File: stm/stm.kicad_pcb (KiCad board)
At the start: 2 copper layers, 28 parts, among them U2 STM32H730ZBTx, U3 LAN8742A, U4 LM1117MP-ADJ, U5 FT232RL

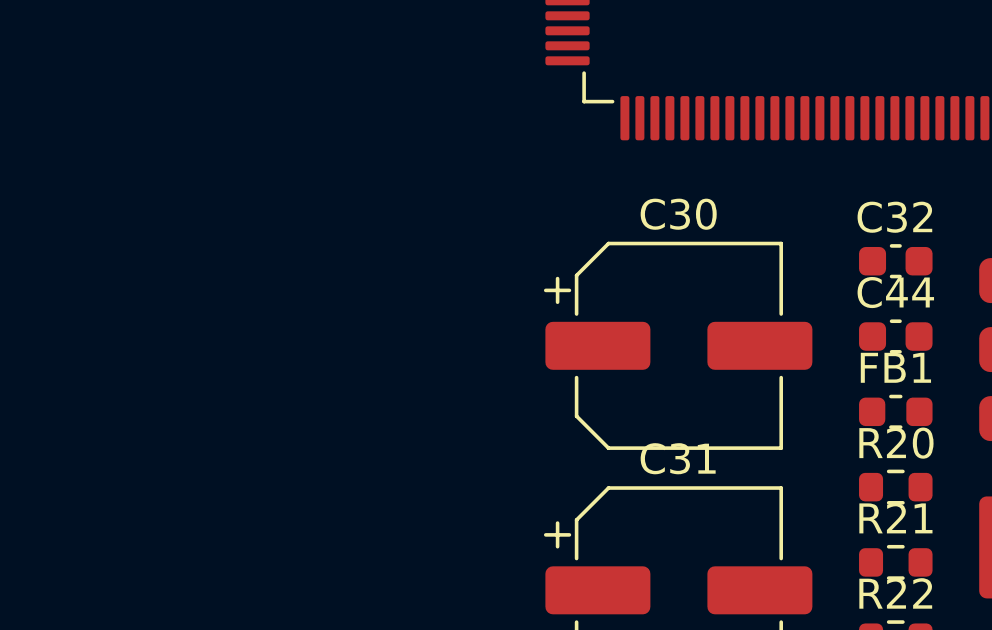
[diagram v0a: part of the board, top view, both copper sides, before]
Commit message: updated DAQ silkscreen to be less dumb
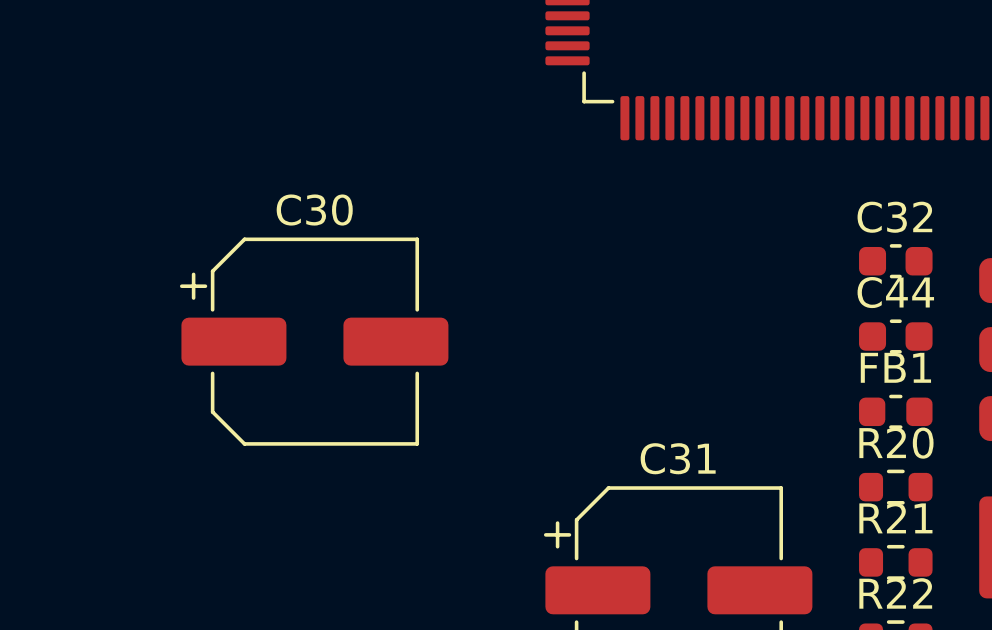
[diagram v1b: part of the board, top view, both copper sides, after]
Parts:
- moved C30 12.1 mm to (95.0, 104.0)
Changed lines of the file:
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@@
 	(footprint "Capacitor_SMD:CP_Elec_6.3x7.7"
 		(layer "F.Cu")
-		(at 107.1325 104.14)
+		(at 95 104)
 		(descr "SMD capacitor, aluminum electrolytic, Nichicon, 6.3x7.7mm")
 		(tags "capacitor electrolytic")

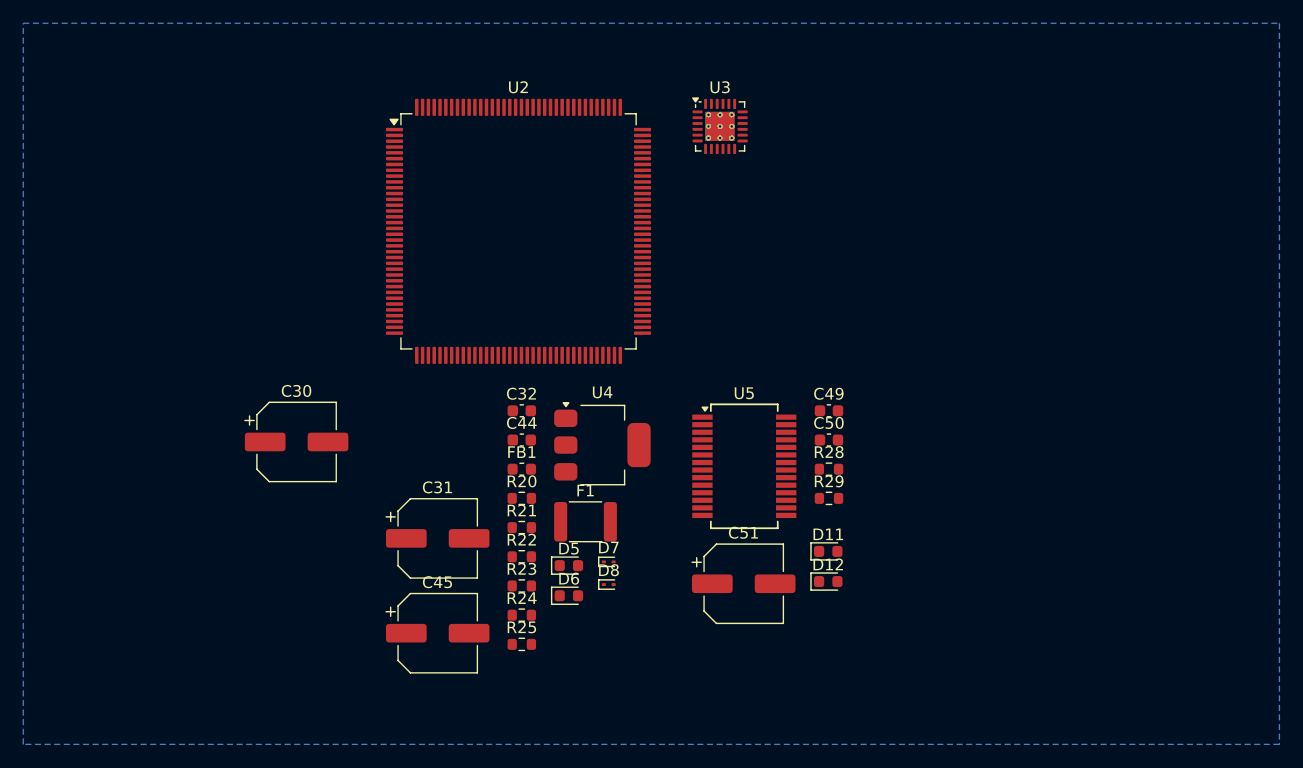
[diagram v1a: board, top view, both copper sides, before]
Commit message: Added components to main libs folder
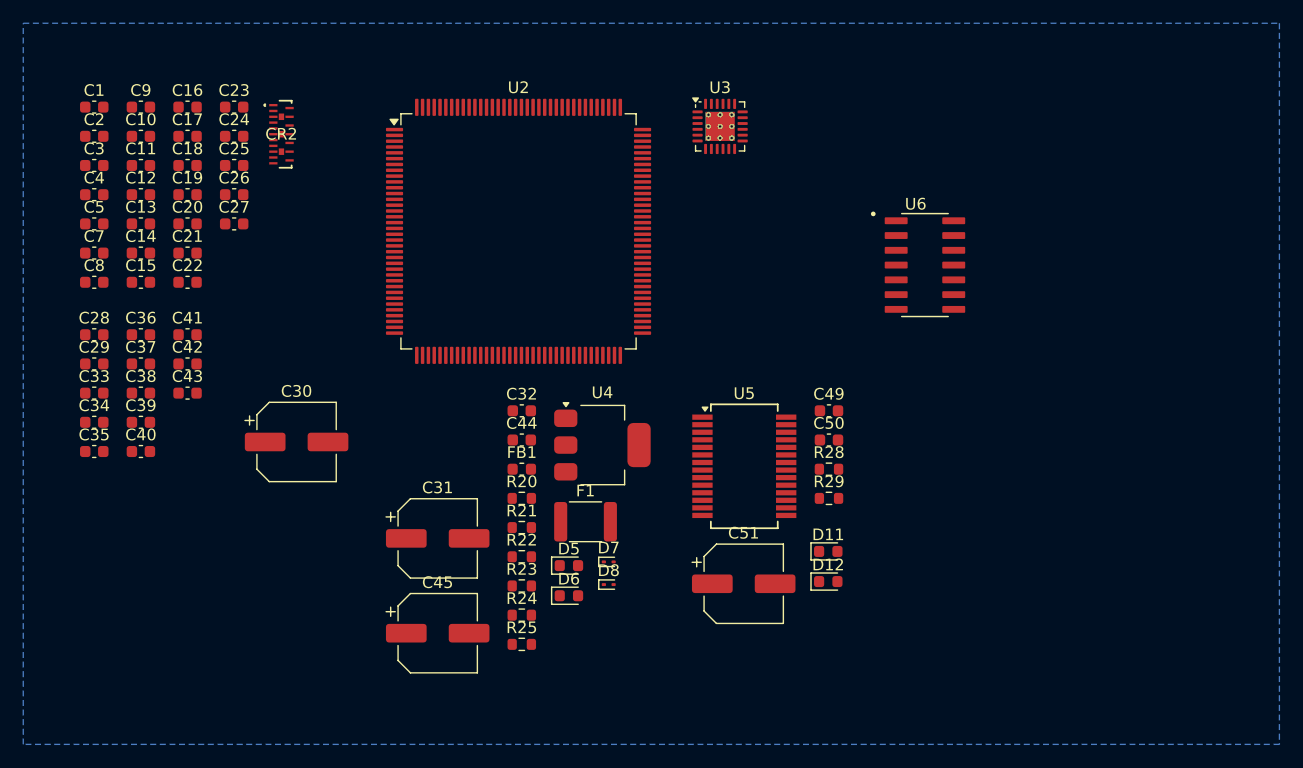
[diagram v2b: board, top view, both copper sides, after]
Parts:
- added C1: 100n, Capacitor_SMD:C_0603_1608Metric, F.Cu at (77.6, 75.2)
- added C10: 100n, Capacitor_SMD:C_0603_1608Metric, F.Cu at (81.6, 77.7)
- added C11: 2.2u, Capacitor_SMD:C_0603_1608Metric, F.Cu at (81.6, 80.2)
- added C12: 2.2u, Capacitor_SMD:C_0603_1608Metric, F.Cu at (81.6, 82.7)
- added C13: 15p, Capacitor_SMD:C_0603_1608Metric, F.Cu at (81.6, 85.2)
- added C14: 15p, Capacitor_SMD:C_0603_1608Metric, F.Cu at (81.6, 87.8)
- added C15: 100n, Capacitor_SMD:C_0603_1608Metric, F.Cu at (81.6, 90.3)
- added C16: 100n, Capacitor_SMD:C_0603_1608Metric, F.Cu at (85.6, 75.2)
- added C17: 100n, Capacitor_SMD:C_0603_1608Metric, F.Cu at (85.6, 77.7)
- added C18: 100n, Capacitor_SMD:C_0603_1608Metric, F.Cu at (85.6, 80.2)
- added C19: 100n, Capacitor_SMD:C_0603_1608Metric, F.Cu at (85.6, 82.7)
- added C2: 1u, Capacitor_SMD:C_0603_1608Metric, F.Cu at (77.6, 77.7)
- added C20: 1u, Capacitor_SMD:C_0603_1608Metric, F.Cu at (85.6, 85.2)
- added C21: 100n, Capacitor_SMD:C_0603_1608Metric, F.Cu at (85.6, 87.8)
- added C22: 100n, Capacitor_SMD:C_0603_1608Metric, F.Cu at (85.6, 90.3)
- added C23: 100n, Capacitor_SMD:C_0603_1608Metric, F.Cu at (89.6, 75.2)
- added C24: 100n, Capacitor_SMD:C_0603_1608Metric, F.Cu at (89.6, 77.7)
- added C25: 100n, Capacitor_SMD:C_0603_1608Metric, F.Cu at (89.6, 80.2)
- added C26: 100n, Capacitor_SMD:C_0603_1608Metric, F.Cu at (89.6, 82.7)
- added C27: 4u7, Capacitor_SMD:C_0603_1608Metric, F.Cu at (89.6, 85.2)
- added C28: C, Capacitor_SMD:C_0603_1608Metric, F.Cu at (77.6, 94.8)
- added C29: C, Capacitor_SMD:C_0603_1608Metric, F.Cu at (77.6, 97.3)
- added C3: 100n, Capacitor_SMD:C_0603_1608Metric, F.Cu at (77.6, 80.2)
- added C33: C, Capacitor_SMD:C_0603_1608Metric, F.Cu at (77.6, 99.8)
- added C34: C, Capacitor_SMD:C_0603_1608Metric, F.Cu at (77.6, 102.3)
- added C35: 470p, Capacitor_SMD:C_0603_1608Metric, F.Cu at (77.6, 104.8)
- added C36: 1u, Capacitor_SMD:C_0603_1608Metric, F.Cu at (81.6, 94.8)
- added C37: 1u, Capacitor_SMD:C_0603_1608Metric, F.Cu at (81.6, 97.3)
- added C38: 1u, Capacitor_SMD:C_0603_1608Metric, F.Cu at (81.6, 99.8)
- added C39: 10p, Capacitor_SMD:C_0603_1608Metric, F.Cu at (81.6, 102.3)
- added C4: 1u, Capacitor_SMD:C_0603_1608Metric, F.Cu at (77.6, 82.7)
- added C40: 10p, Capacitor_SMD:C_0603_1608Metric, F.Cu at (81.6, 104.8)
- added C41: 10p, Capacitor_SMD:C_0603_1608Metric, F.Cu at (85.6, 94.8)
- added C42: 10p, Capacitor_SMD:C_0603_1608Metric, F.Cu at (85.6, 97.3)
- added C43: 0.022u, Capacitor_SMD:C_0603_1608Metric, F.Cu at (85.6, 99.8)
- added C5: 0.1uF, Capacitor_SMD:C_0603_1608Metric, F.Cu at (77.6, 85.2)
- added C7: 100n, Capacitor_SMD:C_0603_1608Metric, F.Cu at (77.6, 87.8)
- added C8: 6p, Capacitor_SMD:C_0603_1608Metric, F.Cu at (77.6, 90.3)
- added C9: 6p, Capacitor_SMD:C_0603_1608Metric, F.Cu at (81.6, 75.2)
- added CR2: ESD7008MUTAG, ESD7008MUTAG:UDFN18_517BV_ONS, F.Cu at (93.7, 77.5)
- added U6: MAX13448EESD_, MAX13448EESD:SOIC127P600X175-14N, F.Cu at (149.0, 88.8)
